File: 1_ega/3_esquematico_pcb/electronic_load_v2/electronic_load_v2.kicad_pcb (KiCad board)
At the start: 2 copper layers, 100 x 50 mm, 68 parts, among them J1 Encoder, J11 LOAD, J12 Memoria SD, J13 LCD, J15 VCC, J16 RTC, J17 EGB, J3 GND, J6 RPico PWR, J7 GND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

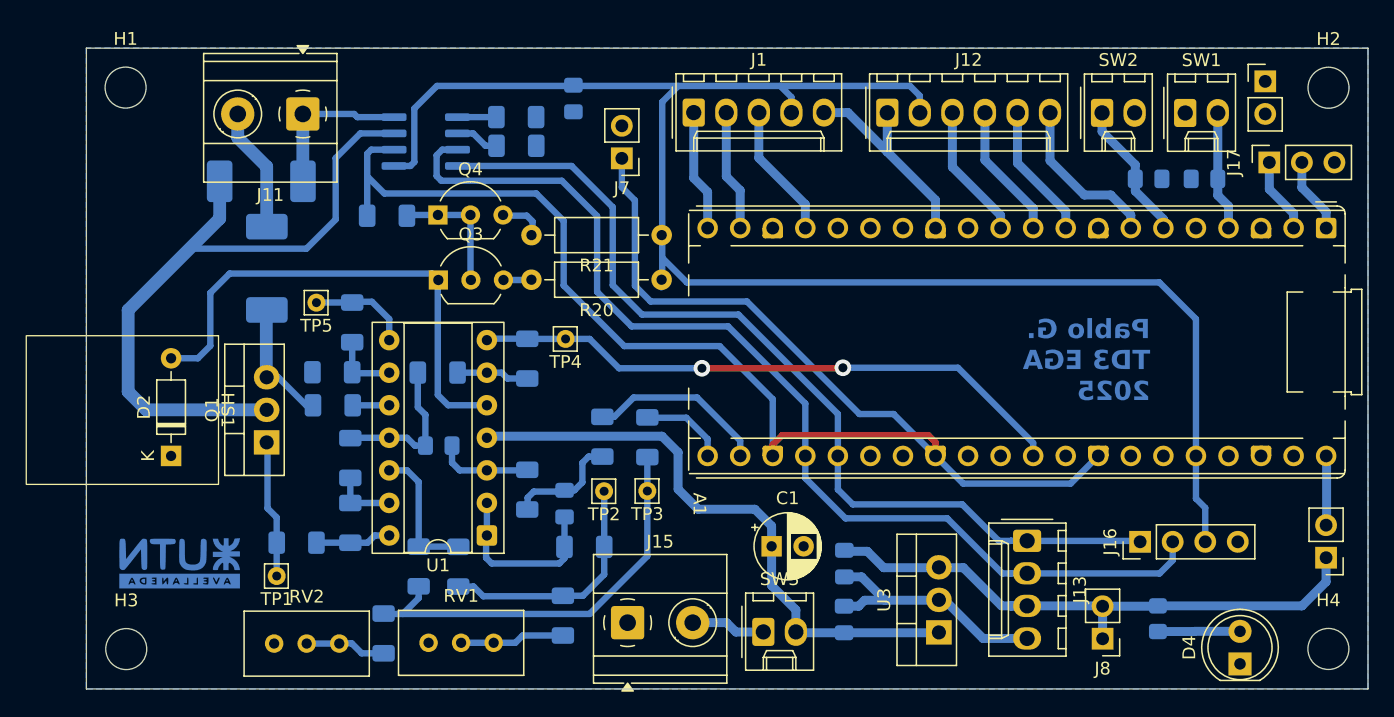
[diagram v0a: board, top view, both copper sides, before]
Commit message: chore: add name and UTN Logo
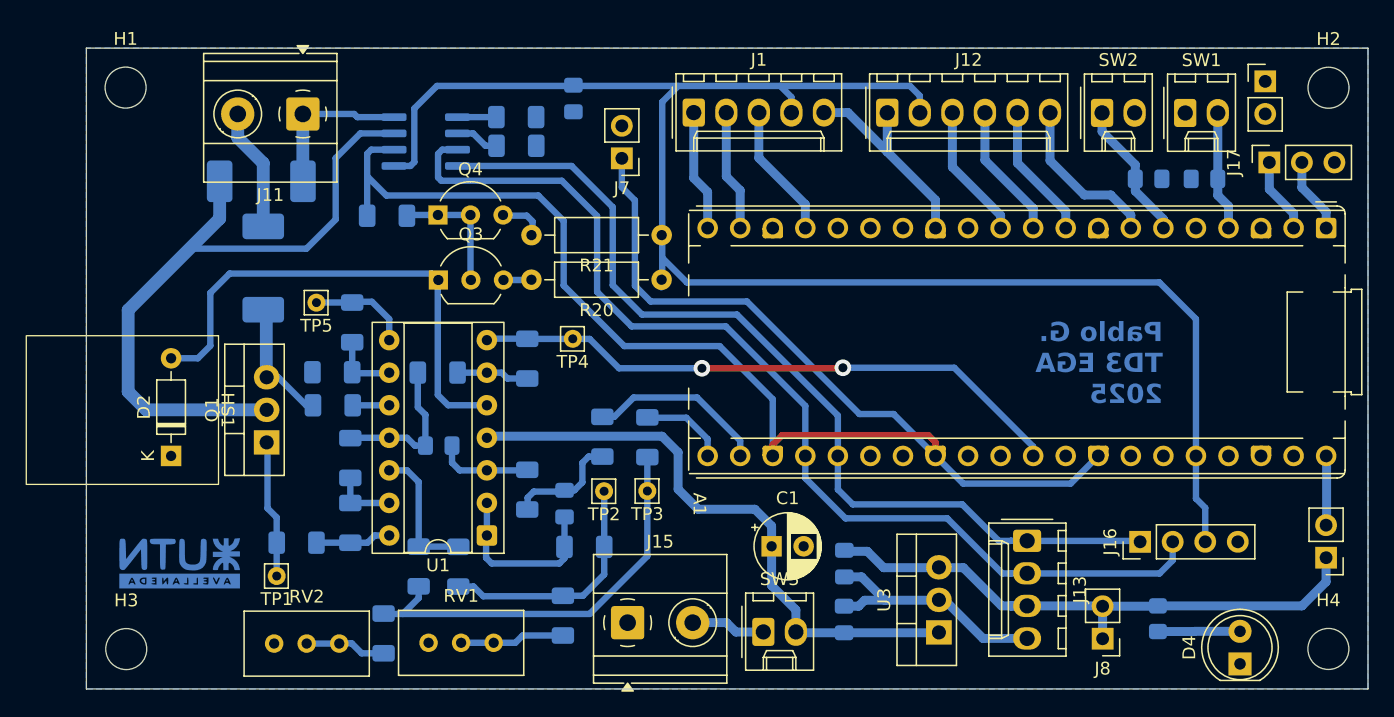
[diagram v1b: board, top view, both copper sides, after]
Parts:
- moved TP4 0.56 mm to (58.0, 80.2)
- moved R1 0.28 mm to (33.8, 74.7)
